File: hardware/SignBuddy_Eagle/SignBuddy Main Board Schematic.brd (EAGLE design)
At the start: 52.8 x 45.9 mm, 42 parts, among them U1 STM32L053C8T6D, U2 NCP115ASN330T2G

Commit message: board done
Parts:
- added 3V3_TP, GND_TP, VBAT_TP: TPB1,27, testpad:B1,27
- moved JP2 194.5 mm to (33.0, 42.5)
- moved R19 169.6 mm to (10.3, 38.4), turned to 270 degrees
- moved C9 166.5 mm to (37.6, 24.9), turned to 180 degrees
- moved R18 166.2 mm to (8.38, 38.4), turned to 270 degrees
- moved C10 163.7 mm to (30.0, 20.3), turned to 180 degrees
- moved C11 162.5 mm to (30.0, 15.7), turned to 180 degrees
- moved R17 159.0 mm to (17.0, 33.8), turned to 270 degrees
- moved R16 155.5 mm to (15.0, 33.8), turned to 270 degrees
- moved C8 155.0 mm to (30.0, 18.0), turned to 180 degrees
- moved R15 152.0 mm to (13.0, 33.8), turned to 270 degrees
- moved R14 148.6 mm to (10.9, 33.8), turned to 270 degrees
- moved R12 147.4 mm to (19.8, 38.4), turned to 270 degrees
- moved R13 145.2 mm to (8.89, 33.8), turned to 270 degrees
- moved R11 143.9 mm to (17.8, 38.4), turned to 270 degrees
- moved R10 140.4 mm to (15.7, 38.4), turned to 270 degrees
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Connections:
- removed net N$3: C6.1, U2.5
- removed net RESET: JP1.4
- net +3V3: now also 3V3_TP.TP, C6.1, U2.5
- net GND: now also GND_TP.TP
- net NRST: now also JP1.4
- net VBAT: now also VBAT_TP.TP
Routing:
- net GND: track 0.00 -> 107.1 mm, vias 0 -> 19
- net ADC_PINKY: track 0.00 -> 92.7 mm, vias 0 -> 2
- net ADC_RING: track 0.00 -> 91.7 mm, vias 0 -> 2
- net ADC_MIDDLE: track 0.00 -> 81.3 mm, vias 0 -> 2
- net TSC_G6_E1: track 0.00 -> 81.1 mm, vias 0 -> 2
- net TSC_G4_E3: track 0.00 -> 79.9 mm, vias 0 -> 4
- net ADC_POINTER: track 0.00 -> 78.4 mm, vias 0 -> 2
- net LOG_UART_TX: track 0.00 -> 78.1 mm
- net ADC_THUMB: track 0.00 -> 68.9 mm, vias 0 -> 2
- net TSC_G2_E1: track 0.00 -> 65.8 mm, vias 0 -> 2
- net TSC_G2_E2: track 0.00 -> 65.0 mm, vias 0 -> 2
- net TSC_G2_E3: track 0.00 -> 64.3 mm, vias 0 -> 4
- net BLE_UART_RX: track 0.00 -> 57.5 mm
- net NRST: track 0.00 -> 51.5 mm
- net TSC_G6_E2: track 0.00 -> 51.1 mm, vias 0 -> 2
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- added copper zone on layer 1, net +3V3
- added copper zone on layer 16, net GND
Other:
- board size 52.8 x 45.9 mm -> 54.1 x 47.4 mm

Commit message: fixes
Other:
- board size 54.1 x 47.4 mm -> 54.1 x 47.5 mm
- board text added: "+"
- board text added: "-"
- board text added: "0"
- board text added: "1"
- board text added: "BLE"
- board text added: "BLE_UART"
- board text added: "BOOT"
- board text added: "CLK"
- board text added: "DIO"
- board text added: "GND"
- board text added: "NRST"
- board text added: "PROG"
- board text added: "RST"
- board text added: "SWCLK"
- board text added: "TX"
- board text added: "VREF"
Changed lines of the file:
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@@
 <board>
 <plain>
-<wire x1="0.254" y1="-0.508" x2="54.324" y2="-0.508" width="0" layer="20"/>
-<wire x1="54.324" y1="-0.508" x2="54.324" y2="46.916" width="0" layer="20"/>
-<wire x1="54.324" y1="46.916" x2="0.254" y2="46.916" width="0" layer="20"/>
-<wire x1="0.254" y1="46.916" x2="0.254" y2="-0.508" width="0" layer="20"/>
+<text x="24.638" y="0" size="1.778" layer="27">+</text>
+<text x="26.924" y="0.127" size="1.778" layer="27">-</text>
+<text x="32.004" y="44.196" size="0.6096" layer="27" rot="R90">TX</text>
+<text x="34.544" y="44.196" size="0.6096" layer="27" rot="R90">GND</text>
+<text x="49.022" y="44.196" size="0.6096" layer="27" rot="R90">GND</text>
+<text x="38.608" y="44.196" size="0.6096" layer="27" rot="R90">VREF</text>
+<text x="41.148" y="44.196" size="0.6096" layer="27" rot="R90">DIO</text>
+<text x="43.688" y="44.196" size="0.6096" layer="27" rot="R90">CLK</text>
+<text x="46.228" y="44.196" size="0.6096" layer="27" rot="R90">RST</text>
+<text x="39.878" y="37.592" size="0.6096" layer="27" rot="R180">BOOT</text>
+<text x="25.654" y="35.56" size="0.6096" layer="27">CLK</text>
+<text x="25.908" y="28.956" size="0.6096" layer="27">BLE</text>
+<text x="29.464" y="37.084" size="0.6096" layer="27">PROG</text>
+<text x="46.736" y="38.1" size="0.6096" layer="27">0</text>
+<text x="47.244" y="28.448" size="0.6096" layer="27">1</text>
+<text x="25.146" y="0.762" size="0.6096" layer="25">+</text>
+<text x="27.178" y="0.762" size="0.6096" layer="25">-</text>
+<text x="32.004" y="44.45" size="0.6096" layer="25" rot="R90">TX</text>
+<text x="34.29" y="44.196" size="0.6096" layer="25" rot="R90">GND</text>
+<text x="48.768" y="44.45" size="0.6096" layer="25" rot="R90">GND</text>
+<text x="38.354" y="43.942" size="0.6096" layer="25" rot="R90">VREF</text>
+<text x="41.148" y="44.196" size="0.6096" layer="25" rot="R90">DIO</text>
+<text x="43.688" y="44.196" size="0.6096" layer="25" rot="R90">CLK</text>
+<text x="46.228" y="44.196" size="0.6096" layer="25" rot="R90">NRST</text>
+<text x="24.13" y="35.56" size="0.6096" layer="25">SWCLK</text>
+<text x="22.86" y="30.226" size="0.6096" layer="25">BLE_UART</text>
+<text x="29.21" y="38.354" size="0.6096" layer="25">PROG</text>
+<text x="38.1" y="38.354" size="0.6096" layer="25">BOOT</text>
+<text x="45.466" y="37.846" size="0.6096" layer="25">0</text>
+<text x="45.72" y="28.448" size="0.6096" layer="25">1</text>
+<wire x1="0.254" y1="45.72" x2="1.524" y2="46.99" width="0" layer="20" curve="-90"/>
+<wire x1="1.524" y1="46.99" x2="52.578" y2="46.99" width="0" layer="20"/>
+<wire x1="52.578" y1="46.99" x2="54.356" y2="45.212" width="0" layer="20" curve="-90"/>
+<wire x1="54.356" y1="45.212" x2="54.356" y2="0.762" width="0" layer="20"/>
+<wire x1="54.356" y1="0.762" x2="53.086" y2="-0.508" width="0" layer="20" curve="-90"/>
+<wire x1="53.086" y1="-0.508" x2="2.032" y2="-0.508" width="0" layer="20"/>
+<wire x1="2.032" y1="-0.508" x2="0.254" y2="1.27" width="0" layer="20" curve="-90"/>
+<wire x1="0.254" y1="1.27" x2="0.254" y2="45.72" width="0" layer="20"/>
 </plain>
 <attributes>
@@
 </element>
 <element name="JP1" library="pinhead" library_urn="urn:adsk.eagle:library:325" package="1X05" package3d_urn="urn:adsk.eagle:package:22469/2" value="" x="43.476" y="42.512" smashed="yes">
-<attribute name="NAME" x="37.0498" y="44.3408" size="1.27" layer="25" ratio="10"/>
 <attribute name="POPULARITY" value="69" x="43.476" y="42.512" size="1.778" layer="27" display="off"/>
 <attribute name="VALUE" x="37.126" y="39.337" size="1.27" layer="27"/>
@@
 <attribute name="MANUFACTURER_PART_NUMBER" value="NCP115ASN330T2G" x="26.67" y="12.192" size="1.778" layer="27" display="off"/>
 <attribute name="MFR_NAME" value="onsemi" x="26.67" y="12.192" size="1.778" layer="27" display="off"/>
-<attribute name="NAME" x="23.3934" y="11.557" size="1.27" layer="27" ratio="6" rot="SR0"/>
-<attribute name="VALUE" x="24.9428" y="11.557" size="1.27" layer="21" ratio="6" rot="SR0"/>
 </element>
 <element name="C6" library="SparkFun-Capacitors" library_urn="urn:adsk.eagle:library:510" package="0603" package3d_urn="urn:adsk.eagle:package:37414/1" value="1uF" x="28.956" y="8.128" smashed="yes" rot="R180">
@@
 <attribute name="VALUE" x="23.368" y="8.636" size="0.6096" layer="27" font="vector" ratio="20" rot="R180" align="top-center"/>
 </element>
-<element name="U$4" library="SRG" package="JST_B2B-PH_HEADER" value="JST-PH_2-PIN_HEADER" x="26.416" y="3.81" smashed="yes" rot="R180">
-<attribute name="NAME" x="29.341" y="1.1275" size="0.8128" layer="25" font="vector" rot="R180"/>
-</element>
+<element name="U$4" library="SRG" package="JST_B2B-PH_HEADER" value="JST-PH_2-PIN_HEADER" x="26.416" y="3.81" smashed="yes" rot="R180"/>
 <element name="U$5" library="BLE_FRIEND" package="BLE_FRIEND" value="BLE_FRIEND" x="12.7" y="4.572" smashed="yes"/>
 <element name="R3" library="SparkFun-Resistors" library_urn="urn:adsk.eagle:library:532" package="0603" package3d_urn="urn:adsk.eagle:package:39650/1" value="10k" x="10.922" y="16.002" smashed="yes" rot="R180">
@@
 </element>
 <element name="JP2" library="pinhead" library_urn="urn:adsk.eagle:library:325" package="1X02" package3d_urn="urn:adsk.eagle:package:22435/2" value="" x="33.02" y="42.545" smashed="yes">
-<attribute name="NAME" x="30.4038" y="44.3738" size="1.27" layer="25" ratio="10"/>
 <attribute name="POPULARITY" value="98" x="33.02" y="42.545" size="1.778" layer="27" display="off"/>
 <attribute name="VALUE" x="30.48" y="39.37" size="1.27" layer="27"/>
 </element>
 <element name="VBAT_TP" library="testpad" library_urn="urn:adsk.eagle:library:385" package="B1,27" package3d_urn="urn:adsk.eagle:package:27944/2" value="TPB1,27" x="25.4" y="15.24" smashed="yes" rot="MR0">
-<attribute name="NAME" x="26.035" y="16.256" size="1.27" layer="26" ratio="10" rot="MR0"/>
+<attribute name="NAME" x="24.003" y="14.732" size="1.27" layer="26" ratio="10" rot="MR0"/>
 <attribute name="POPULARITY" value="19" x="25.4" y="15.24" size="1.778" layer="28" rot="MR0" display="off"/>
 <attribute name="TP_SIGNAL_NAME" value="" x="25.4" y="15.24" size="1.778" layer="28" rot="MR0" display="off"/>
@@
 </element>
 <element name="3V3_TP" library="testpad" library_urn="urn:adsk.eagle:library:385" package="B1,27" package3d_urn="urn:adsk.eagle:package:27944/2" value="TPB1,27" x="29.972" y="10.668" smashed="yes" rot="MR0">
-<attribute name="NAME" x="30.607" y="11.684" size="1.27" layer="26" ratio="10" rot="MR0"/>
+<attribute name="NAME" x="28.829" y="10.16" size="1.27" layer="26" ratio="10" rot="MR0"/>
 <attribute name="POPULARITY" value="19" x="29.972" y="10.668" size="1.778" layer="28" rot="MR0" display="off"/>
 <attribute name="TP_SIGNAL_NAME" value="" x="29.972" y="10.668" size="1.778" layer="28" rot="MR0" display="off"/>
@@
 </element>
 <element name="GND_TP" library="testpad" library_urn="urn:adsk.eagle:library:385" package="B1,27" package3d_urn="urn:adsk.eagle:package:27944/2" value="TPB1,27" x="32.004" y="8.636" smashed="yes" rot="MR0">
-<attribute name="NAME" x="32.639" y="9.652" size="1.27" layer="26" ratio="10" rot="MR0"/>
+<attribute name="NAME" x="30.861" y="7.874" size="1.27" layer="26" ratio="10" rot="MR0"/>
 <attribute name="POPULARITY" value="19" x="32.004" y="8.636" size="1.778" layer="28" rot="MR0" display="off"/>
 <attribute name="TP_SIGNAL_NAME" value="" x="32.004" y="8.636" size="1.778" layer="28" rot="MR0" display="off"/>

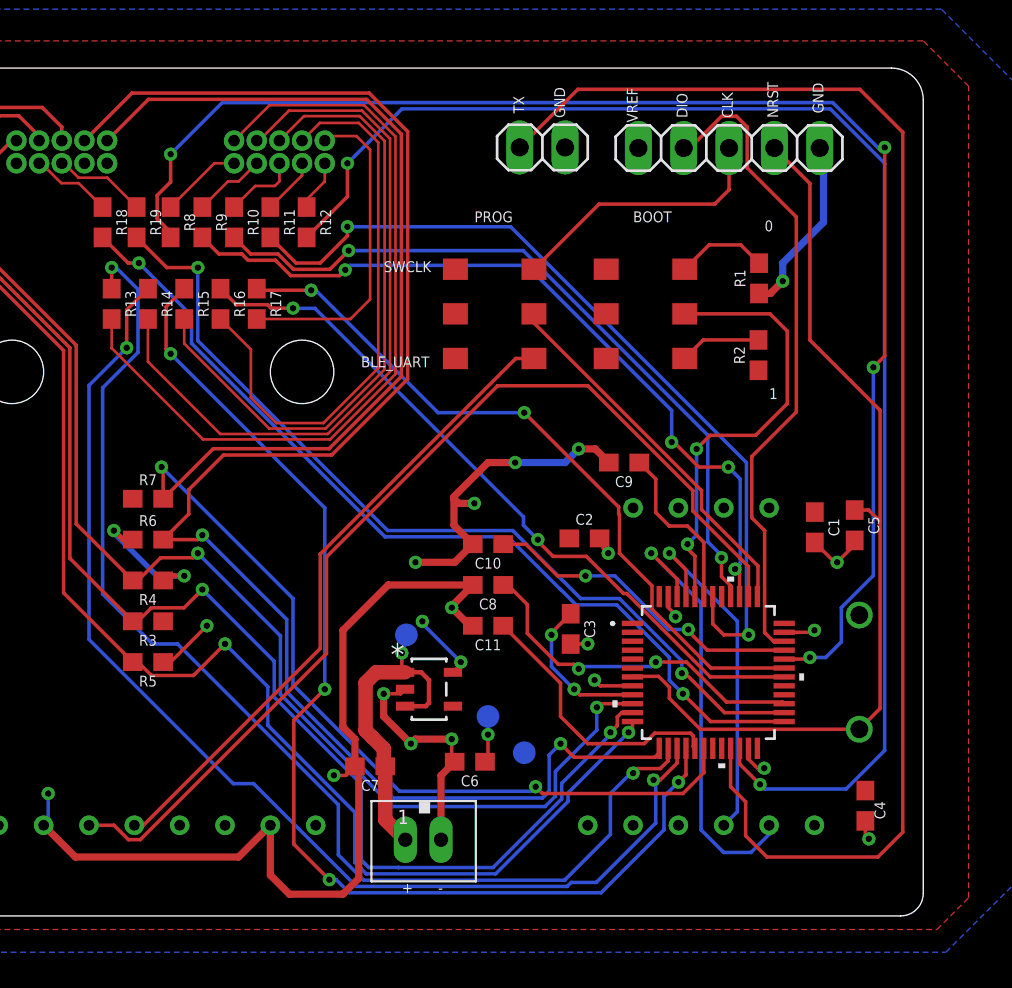
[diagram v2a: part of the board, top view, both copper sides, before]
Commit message: Add status led and adc test point (#124)
* Add status led and adc test point

* fixes

Co-authored-by: Adam Bujak <adamjbujak@gmail.com>
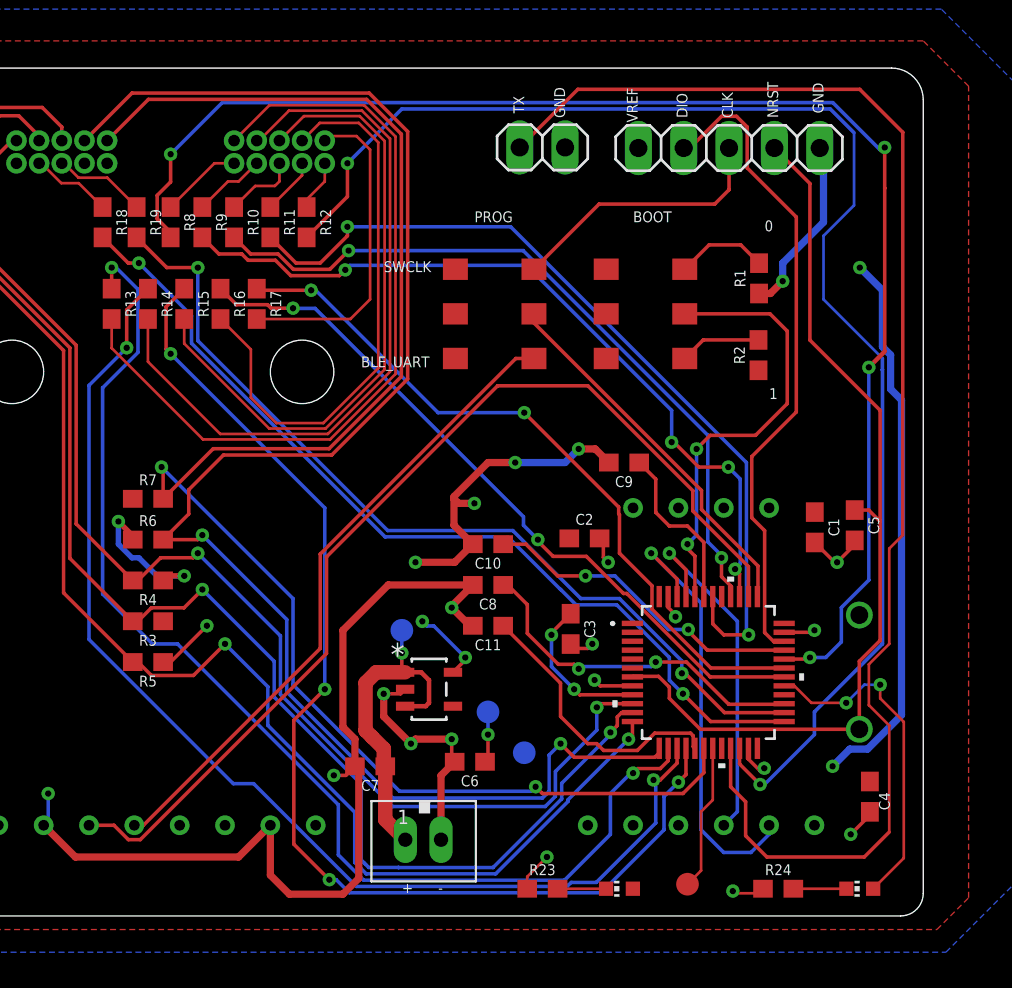
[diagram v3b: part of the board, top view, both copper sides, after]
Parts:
- added ADC_TP: TPB1,27, testpad:B1,27
- added LED1, LED2: (no value), led:CHIP-LED0603
- added R23, R24: 1k, SparkFun-Resistors:0603
- moved C4 0.57 mm to (51.4, 6.17)
- moved VBAT_TP 0.36 mm to (25.1, 15.5)
- moved 3V3_TP 0.25 mm to (30.0, 10.9)
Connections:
- new net LED: LED2.A, U1.29
- new net N$17: LED1.C, R23.2
- new net N$3: LED2.C, R24.2
- net +3V3: now also LED1.A
- net ADC_EXTRA: now also ADC_TP.TP
- net GND: now also R23.1, R24.1
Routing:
- net +3V3: track 26.2 -> 58.5 mm, vias 8 -> 10
- net LED: track 0.00 -> 19.3 mm, vias 0 -> 2
- net ADC_EXTRA: track 0.00 -> 8.20 mm
- net GND: track 107.1 -> 112.9 mm, vias 19 -> 21
- net N$3: track 0.00 -> 2.97 mm
- net N$17: track 0.00 -> 2.72 mm
- net TSC_G6_E1: track 81.1 -> 79.4 mm
- net LOG_UART_TX: track 78.1 -> 78.6 mm

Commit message: fixups
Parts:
- moved C9 0.54 mm to (37.2, 24.5)
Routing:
- net BOOT0: track 25.0 -> 17.8 mm
- net TSC_G5_E1: track 44.1 -> 42.9 mm, vias 4 -> 2
- net GND: track 112.9 -> 113.9 mm
- net SWCLK/BLE_UART_TX: track 21.1 -> 21.6 mm

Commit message: small position adjustments
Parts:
- moved C1 4.32 mm to (50.3, 25.1)
- moved C2 3.81 mm to (32.3, 22.9)
- moved C9 1.98 mm to (35.7, 25.8)
- moved C5 0.22 mm to (50.3, 21.3)
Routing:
- net GND: track 113.9 -> 116.2 mm
- net TSC_G5_SAMPLER: track 9.38 -> 11.3 mm
- net TSC_G4_E2: track 40.3 -> 39.6 mm
- net TSC_G4_E1: track 40.9 -> 41.5 mm
